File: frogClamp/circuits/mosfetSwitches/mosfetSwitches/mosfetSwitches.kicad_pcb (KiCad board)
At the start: 2 copper layers, 26 x 22 mm, 11 parts, among them Q1 IRLR8726, Q2 IRLR8726

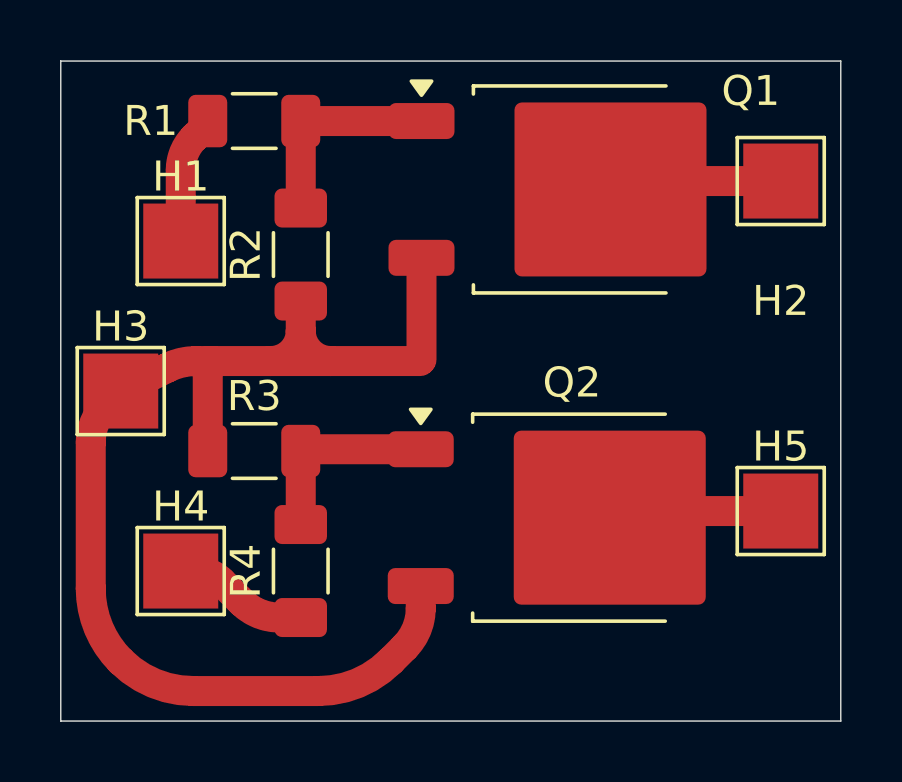
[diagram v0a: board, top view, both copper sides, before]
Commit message: Updated parsing of footprints to include holes and 90 degree rotations.
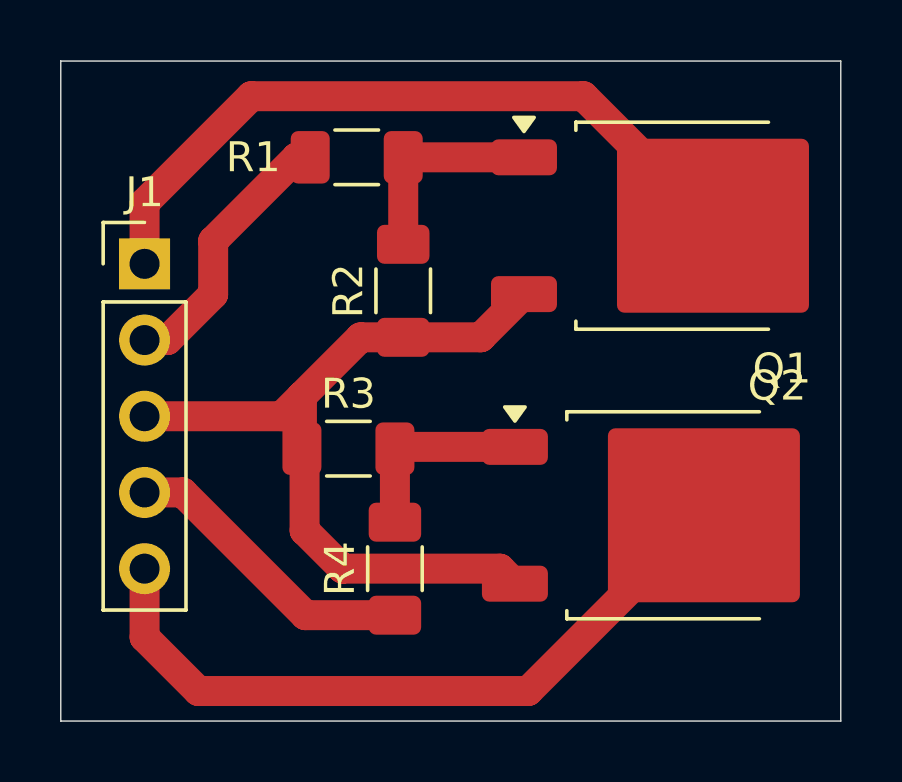
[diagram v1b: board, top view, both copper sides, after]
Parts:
- removed H1, H2, H3, H4, H5: pad, TestPoint:TestPoint_Pad_2.5x2.5mm
- added J1: Conn_01x05_Pin, Connector_PinHeader_2.54mm:PinHeader_1x05_P2.54mm_Vertical, F.Cu at (139.8, 84.8)
- moved R1 3.62 mm to (146.9, 81.2)
- moved Q1 3.62 mm to (157.5, 83.5)
- moved R2 3.62 mm to (148.4, 85.7)
- moved Q2 3.14 mm to (157.2, 93.1)
- moved R3 3.14 mm to (146.6, 90.9)
- moved R4 3.14 mm to (148.1, 94.9)
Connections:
- Q1 pad 2: Net-(Q1-D) -> /MOT1
- Q2 pad 2: Net-(Q2-D) -> /MOT2
- R1 pad 1: Net-(H1-Pad1) -> /IN1
- R4 pad 1: Net-(H4-Pad1) -> /IN2
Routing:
- net /MOT1: track 0.00 -> 24.2 mm
- net /MOT2: track 0.00 -> 24.1 mm
- net GND: track 42.7 -> 26.6 mm
- net /IN2: track 0.00 -> 10.0 mm
- net /IN1: track 0.00 -> 9.09 mm
- net Net-(Q2-D): track 5.77 -> 0.00 mm
- net Net-(Q1-D): track 5.77 -> 0.00 mm
- net Net-(H4-Pad1): track 4.50 -> 0.00 mm
- net Net-(H1-Pad1): track 4.29 -> 0.00 mm

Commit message: made mosfet board curvy lines.
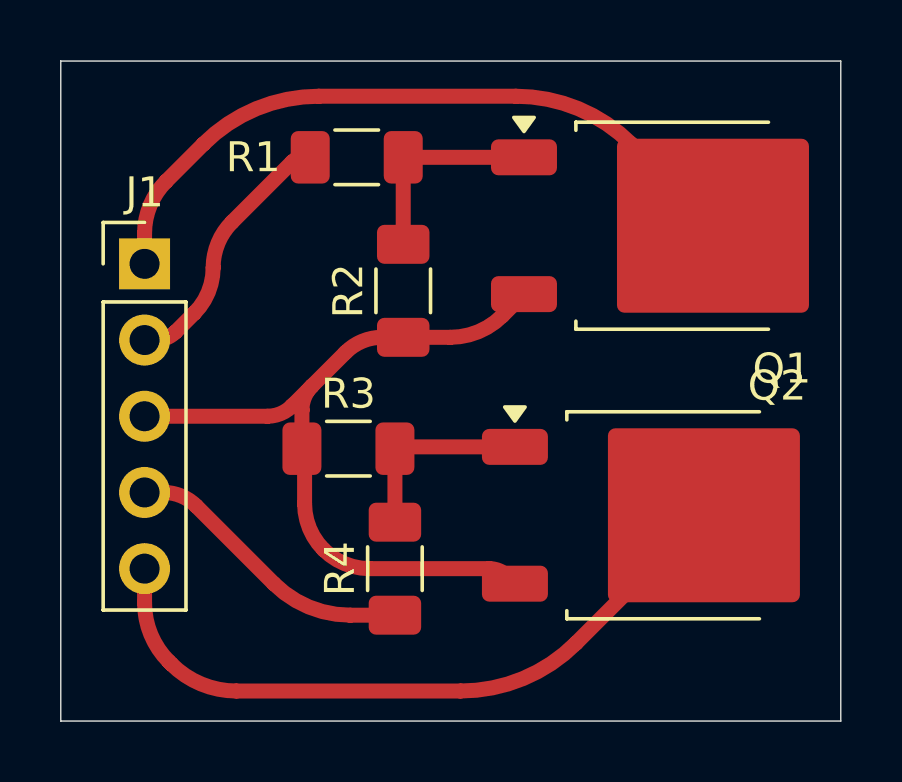
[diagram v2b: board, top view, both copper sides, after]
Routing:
- net /MOT1: track 24.2 -> 23.6 mm
- net /MOT2: track 24.1 -> 23.6 mm
